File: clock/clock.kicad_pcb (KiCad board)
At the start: 2 copper layers, 100 x 50 mm, 81 parts, among them J1 FTDI, J2 USB, J3 TP, SW1 SW_SPST, SW2 SW_SPST, SW3 SW_SPST, SW4 SW_SPST, SW5 SW_SPST, U1 iv12, U10 PCA9685PW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

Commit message: Clean up
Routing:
- net Net-(R16-Pad2): track 15.8 -> 17.4 mm
- net +5V: track 288.8 -> 287.9 mm
- net Net-(R20-Pad2): track 14.1 -> 14.6 mm

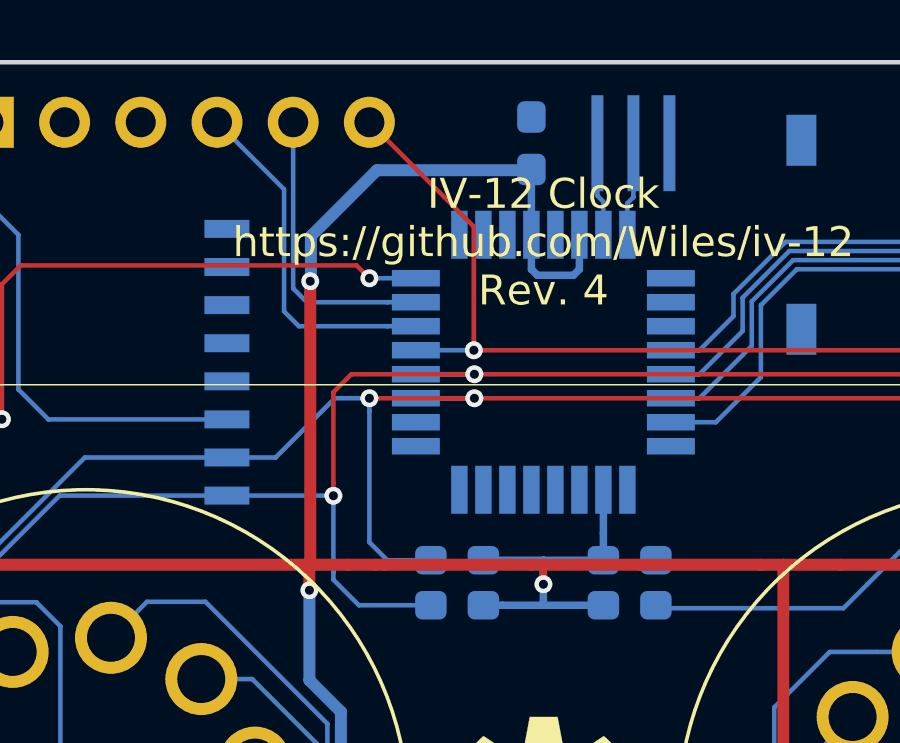
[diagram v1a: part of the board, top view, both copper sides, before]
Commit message: Fixed crystal pinout
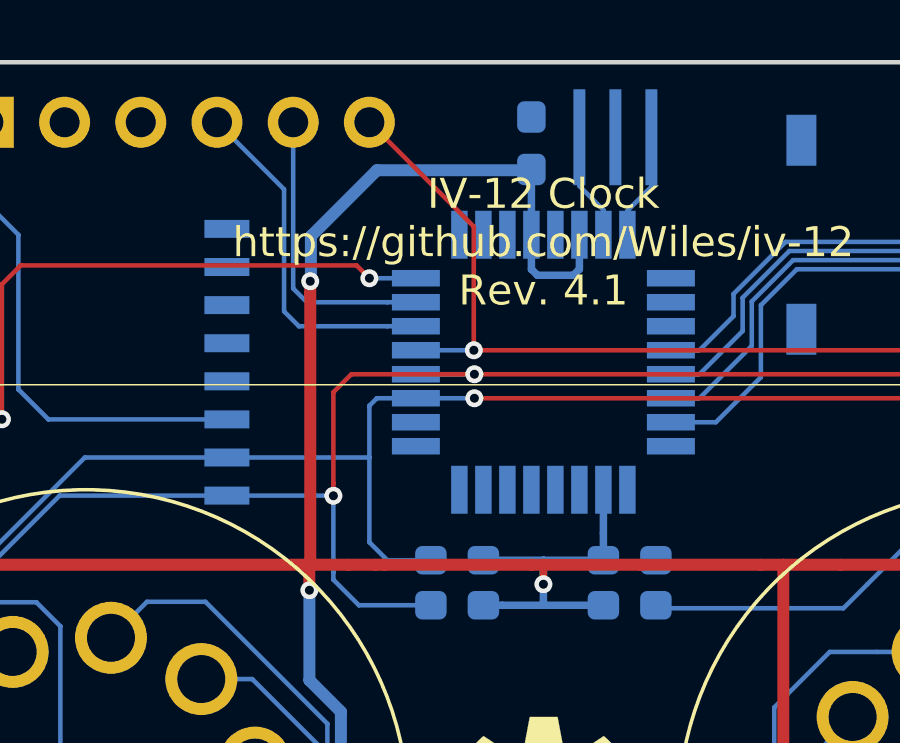
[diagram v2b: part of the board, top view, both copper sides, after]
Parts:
- BT1: value 3v -> CR1220
- R29, R30, R31, R32: value R_Small -> 27
- Y1: value 16MHz -> 16 MHz
- moved Y1 0.63 mm to (129.4, 104.5), turned to 180 degrees
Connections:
- Y1 pad 1: Net-(U11-Pad7) -> Net-(U11-Pad8)
- Y1 pad 2: Net-(U11-Pad8) -> GND
- Y1 pad 3: GND -> Net-(U11-Pad7)
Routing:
- net SDA: track 126.4 -> 123.5 mm, vias 3 -> 2
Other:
- board text added: "IV-12 Clock https://github.com/Wiles/iv-12 Rev. 4.1"
- board text removed: "IV-12 Clock https://github.com/Wiles/iv-12 Rev. 4"

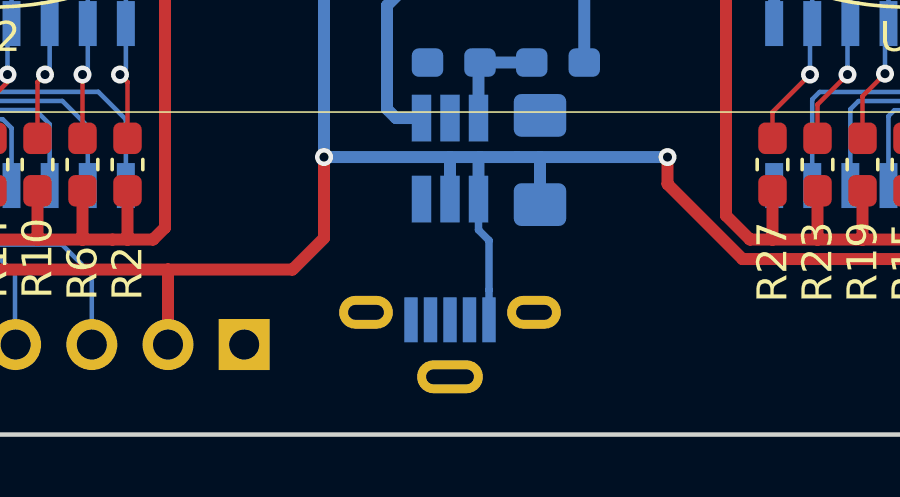
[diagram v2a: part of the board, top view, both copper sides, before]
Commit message: Changed USB footprint
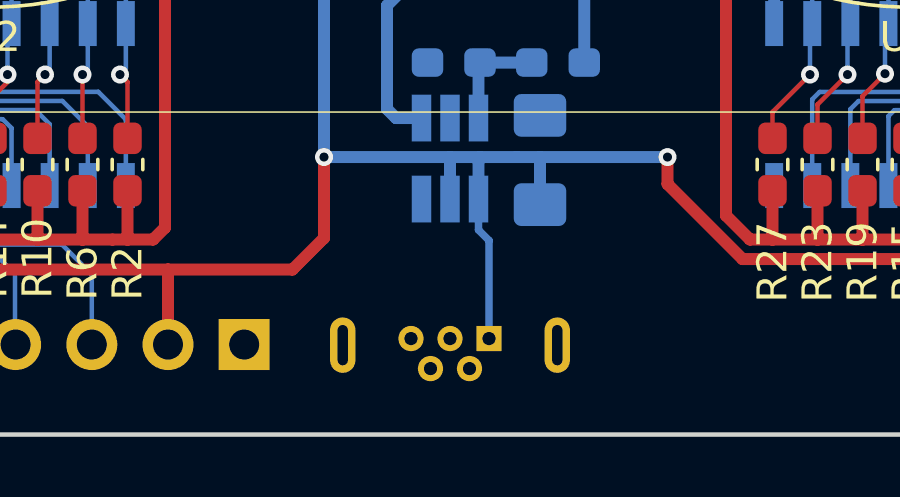
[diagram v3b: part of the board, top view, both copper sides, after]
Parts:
- J2: footprint Connector_USB:USB_Micro-B_Molex-105133-0001 -> Connector_USB:USB_Micro-B_Wuerth_614105150721_Vertical
- moved J2 1.32 mm to (128.3, 148.8)
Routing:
- net +5V: track 287.9 -> 288.5 mm
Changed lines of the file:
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@@
     (thickness 1.6)
     (drawings 16)
-    (tracks 907)
+    (tracks 906)
     (zones 0)
     (modules 81)
@@
     )
   )
-  (module Connector_USB:USB_Micro-B_Molex-105133-0001 (layer B.Cu)
-    (at 127 149 180)
-    (descr "Molex Vertical Micro USB Typ-B (http://www.molex.com/pdm_docs/sd/1051330001_sd.pdf)")
-    (tags "Micro-USB SMD Typ-B Vertical")
-    (attr smd)
-    (fp_text reference J2 (at 0 2.85) (layer B.SilkS) hide
-      (effects (font (size 1 1) (thickness 0.15)) (justify mirror))
-    )
-    (fp_text value USB (at -0.025 -3 180) (layer B.Fab)
-      (effects (font (size 1 1) (thickness 0.15)) (justify mirror))
-    )
-    (fp_text user %R (at 0 0.375 180) (layer B.Fab)
-      (effects (font (size 1 1) (thickness 0.15)) (justify mirror))
-    )
-    (fp_line (start -4 -1.565) (end -4 1.435) (layer B.Fab) (width 0.1))
-    (fp_line (start 4 -1.565) (end 4 1.435) (layer B.Fab) (width 0.1))
-    (fp_line (start -4 -1.565) (end 4 -1.565) (layer B.Fab) (width 0.1))
-    (fp_line (start 4 1.435) (end -4 1.435) (layer B.Fab) (width 0.1))
-    (fp_line (start -1.7 1.075) (end -1.7 1.825) (layer B.SilkS) (width 0.12))
-    (fp_line (start -1.7 1.825) (end -1.1 1.825) (layer B.SilkS) (width 0.12))
-    (fp_line (start -2 1.825) (end -4.15 1.825) (layer B.SilkS) (width 0.12))
-    (fp_line (start 4.15 1.825) (end 4.15 -1.725) (layer B.SilkS) (width 0.12))
-    (fp_line (start -4.15 -1.725) (end -1.25 -1.725) (layer B.SilkS) (width 0.12))
-    (fp_line (start -4.15 1.825) (end -4.15 -1.725) (layer B.SilkS) (width 0.12))
-    (fp_line (start 4.15 -1.725) (end 1.25 -1.725) (layer B.SilkS) (width 0.12))
-    (fp_line (start 2 1.825) (end 4.15 1.825) (layer B.SilkS) (width 0.12))
-    (fp_line (start -1.3 1.675) (end -1.525 1.85) (layer B.Fab) (width 0.1))
-    (fp_line (start -1.525 2.075) (end -1.075 2.075) (layer B.Fab) (width 0.1))
-    (fp_line (start -1.3 1.675) (end -1.075 1.85) (layer B.Fab) (width 0.1))
-    (fp_line (start -1.525 1.85) (end -1.525 2.075) (layer B.Fab) (width 0.1))
-    (fp_line (start -1.075 2.075) (end -1.075 1.85) (layer B.Fab) (width 0.1))
-    (fp_line (start -4.5 -2.13) (end -4.5 2.13) (layer B.CrtYd) (width 0.05))
-    (fp_line (start -4.5 2.13) (end 4.5 2.13) (layer B.CrtYd) (width 0.05))
-    (fp_line (start -4.5 -2.13) (end 4.5 -2.13) (layer B.CrtYd) (width 0.05))
-    (fp_line (start 4.5 -2.13) (end 4.5 2.13) (layer B.CrtYd) (width 0.05))
-    (pad 3 smd rect (at 0 0.825 180) (size 0.45 1.5) (layers B.Cu B.Paste B.Mask)
-      (net 94 "Net-(J2-Pad3)"))
-    (pad 4 smd rect (at 0.65 0.825 180) (size 0.45 1.5) (layers B.Cu B.Paste B.Mask)
-      (net 1 GND))
-    (pad 2 smd rect (at -0.65 0.825 180) (size 0.45 1.5) (layers B.Cu B.Paste B.Mask)
-      (net 105 "Net-(J2-Pad2)"))
-    (pad 5 smd rect (at 1.3 0.825 180) (size 0.45 1.5) (layers B.Cu B.Paste B.Mask)
-      (net 1 GND))
-    (pad 1 smd rect (at -1.3 0.825 180) (size 0.45 1.5) (layers B.Cu B.Paste B.Mask)
-      (net 31 +5V))
-    (pad 6 thru_hole oval (at -2.8 1.075 180) (size 1.8 1.1) (drill oval 1.2 0.5) (layers *.Cu *.Mask)
-      (net 1 GND))
-    (pad 6 thru_hole oval (at 2.8 1.075 180) (size 1.8 1.1) (drill oval 1.2 0.5) (layers *.Cu *.Mask)
-      (net 1 GND))
-    (pad 6 thru_hole oval (at 0 -1.075 180) (size 2.2 1.1) (drill oval 1.6 0.5) (layers *.Cu *.Mask)
-      (net 1 GND))
-    (model ${KISYS3DMOD}/Connector_USB.3dshapes/USB_Micro-B_Molex-105133-0001.wrl
-      (at (xyz 0 0 0))
-      (scale (xyz 1 1 1))
-      (rotate (xyz 0 0 0))
-    )
-  )
   (module Connector_PinHeader_2.54mm:PinHeader_1x05_P2.54mm_Vertical (layer B.Cu)
     (at 120.14 149 90)
@@
     )
   )
+  (module Connector_USB:USB_Micro-B_Wuerth_614105150721_Vertical (layer B.Cu)
+    (at 128.3 148.8 180)
+    (descr "USB Micro-B receptacle, through-hole, vertical, http://katalog.we-online.de/em/datasheet/614105150721.pdf")
+    (tags "usb micro receptacle vertical")
+    (fp_text reference J2 (at 1.3 2.48 180) (layer B.SilkS)
+      (effects (font (size 1 1) (thickness 0.15)) (justify mirror))
+    )
+    (fp_text value USB (at 1.3 -2.92 180) (layer B.Fab)
+      (effects (font (size 1 1) (thickness 0.15)) (justify mirror))
+    )
+    (fp_line (start -2.7 1.23) (end -1 1.23) (layer B.Fab) (width 0.15))
+    (fp_line (start -1 1.23) (end 0 0.23) (layer B.Fab) (width 0.15))
+    (fp_line (start 0 0.23) (end 1 1.23) (layer B.Fab) (width 0.15))
+    (fp_line (start 1 1.23) (end 5.3 1.23) (layer B.Fab) (width 0.15))
+    (fp_line (start 5.3 1.23) (end 5.3 -1.67) (layer B.Fab) (width 0.15))
+    (fp_line (start 5.3 -1.67) (end -2.7 -1.67) (layer B.Fab) (width 0.15))
+    (fp_line (start -2.7 -1.67) (end -2.7 1.23) (layer B.Fab) (width 0.15))
+    (fp_line (start -2.85 0.905) (end -2.85 1.38) (layer B.SilkS) (width 0.15))
+    (fp_line (start -2.85 1.38) (end 5.45 1.38) (layer B.SilkS) (width 0.15))
+    (fp_line (start 5.45 1.38) (end 5.45 0.905) (layer B.SilkS) (width 0.15))
+    (fp_line (start -2.85 -1.345) (end -2.85 -1.82) (layer B.SilkS) (width 0.15))
+    (fp_line (start -2.85 -1.82) (end 5.45 -1.82) (layer B.SilkS) (width 0.15))
+    (fp_line (start 5.45 -1.82) (end 5.45 -1.345) (layer B.SilkS) (width 0.15))
+    (fp_line (start -1 1.68) (end 1 1.68) (layer B.SilkS) (width 0.15))
+    (fp_line (start -3.2 1.73) (end -3.2 -2.17) (layer B.CrtYd) (width 0.05))
+    (fp_line (start -3.2 -2.17) (end 5.8 -2.17) (layer B.CrtYd) (width 0.05))
+    (fp_line (start 5.8 -2.17) (end 5.8 1.73) (layer B.CrtYd) (width 0.05))
+    (fp_line (start 5.8 1.73) (end -3.2 1.73) (layer B.CrtYd) (width 0.05))
+    (fp_text user %R (at 1.3 -0.22 180) (layer B.Fab)
+      (effects (font (size 1 1) (thickness 0.15)) (justify mirror))
+    )
+    (pad 1 thru_hole rect (at 0 0 180) (size 0.84 0.84) (drill 0.44) (layers *.Cu *.Mask)
+      (net 31 +5V))
+    (pad 2 thru_hole circle (at 0.65 -1 180) (size 0.84 0.84) (drill 0.44) (layers *.Cu *.Mask)
+      (net 105 "Net-(J2-Pad2)"))
+    (pad 3 thru_hole circle (at 1.3 0 180) (size 0.84 0.84) (drill 0.44) (layers *.Cu *.Mask)
+      (net 94 "Net-(J2-Pad3)"))
+    (pad 4 thru_hole circle (at 1.95 -1 180) (size 0.84 0.84) (drill 0.44) (layers *.Cu *.Mask)
+      (net 1 GND))
+    (pad 5 thru_hole circle (at 2.6 0 180) (size 0.84 0.84) (drill 0.44) (layers *.Cu *.Mask)
+      (net 1 GND))
+    (pad 6 thru_hole oval (at -2.275 -0.22 180) (size 0.85 1.85) (drill oval 0.35 1.35) (layers *.Cu *.Mask)
+      (net 1 GND))
+    (pad 6 thru_hole oval (at 4.875 -0.22 180) (size 0.85 1.85) (drill oval 0.35 1.35) (layers *.Cu *.Mask)
+      (net 1 GND))
+    (model ${KISYS3DMOD}/Connector_USB.3dshapes/USB_Micro-B_Wuerth_614105150721_Vertical.wrl
+      (at (xyz 0 0 0))
+      (scale (xyz 1 1 1))
+      (rotate (xyz 0 0 0))
+    )
+  )
   (gr_text + (at 133.5 124.2) (layer B.SilkS)
     (effects (font (size 1 1) (thickness 0.15)) (justify mirror))
@@
   (segment (start 121.4 118.75) (end 121.7 118.75) (width 0.4) (layer F.Cu) (net 31))
   (segment (start 120.5 118.75) (end 121.4 118.75) (width 0.4) (layer F.Cu) (net 31))
-  (segment (start 128.3 147.175) (end 128.3 148.175) (width 0.25) (layer B.Cu) (net 31))
-  (segment (start 128.3 145.53) (end 128.3 147.175) (width 0.25) (layer B.Cu) (net 31))
   (segment (start 127.95 145.18) (end 128.3 145.53) (width 0.25) (layer B.Cu) (net 31))
   (segment (start 127.95 144.15) (end 127.95 145.18) (width 0.25) (layer B.Cu) (net 31))
@@
   (segment (start 81 127) (end 80 126) (width 0.4) (layer F.Cu) (net 31))
   (via (at 122.8 142.749984) (size 0.6) (drill 0.3) (layers F.Cu B.Cu) (net 31))
-  (segment (start 123.224264 142.749984) (end 122.8 142.749984) (width 0.4) (layer B.Cu) (net 31))
-  (segment (start 126.999984 142.749984) (end 123.224264 142.749984) (width 0.4) (layer B.Cu) (net 31))
   (segment (start 127 142.75) (end 126.999984 142.749984) (width 0.4) (layer B.Cu) (net 31))
   (segment (start 121.7 118.75) (end 126.6 118.75) (width 0.4) (layer F.Cu) (net 31))
@@
   (segment (start 134.25 142.75) (end 134.25 143.65) (width 0.4) (layer F.Cu) (net 31))
   (segment (start 134.25 143.65) (end 136.75 146.15) (width 0.4) (layer F.Cu) (net 31))
+  (segment (start 126.999984 142.749984) (end 123.224264 142.749984) (width 0.4) (layer B.Cu) (net 31))
+  (segment (start 123.224264 142.749984) (end 122.8 142.749984) (width 0.4) (layer B.Cu) (net 31))
+  (segment (start 128.3 148.8) (end 128.3 145.53) (width 0.25) (layer B.Cu) (net 31))
   (segment (start 143.125 132.776301) (end 143.0861 132.815201) (width 0.152) (layer B.Cu) (net 32) (status 30))
   (segment (start 143.125 128.5) (end 143.125 132.776301) (width 0.152) (layer B.Cu) (net 32) (status 30))

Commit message: Label Tx and Rx pins
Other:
- board text added: "R"
- board text added: "T"
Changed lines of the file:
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@@
   (general
     (thickness 1.6)
-    (drawings 16)
+    (drawings 18)
     (tracks 906)
     (zones 0)
@@
     )
   )
+  (gr_text R (at 116.1 106 90) (layer B.SilkS)
+    (effects (font (size 1 1) (thickness 0.15)) (justify mirror))
+  )
+  (gr_text T (at 118.7 106 90) (layer B.SilkS)
+    (effects (font (size 1 1) (thickness 0.15)) (justify mirror))
+  )
   (gr_text + (at 133.5 124.2) (layer B.SilkS)

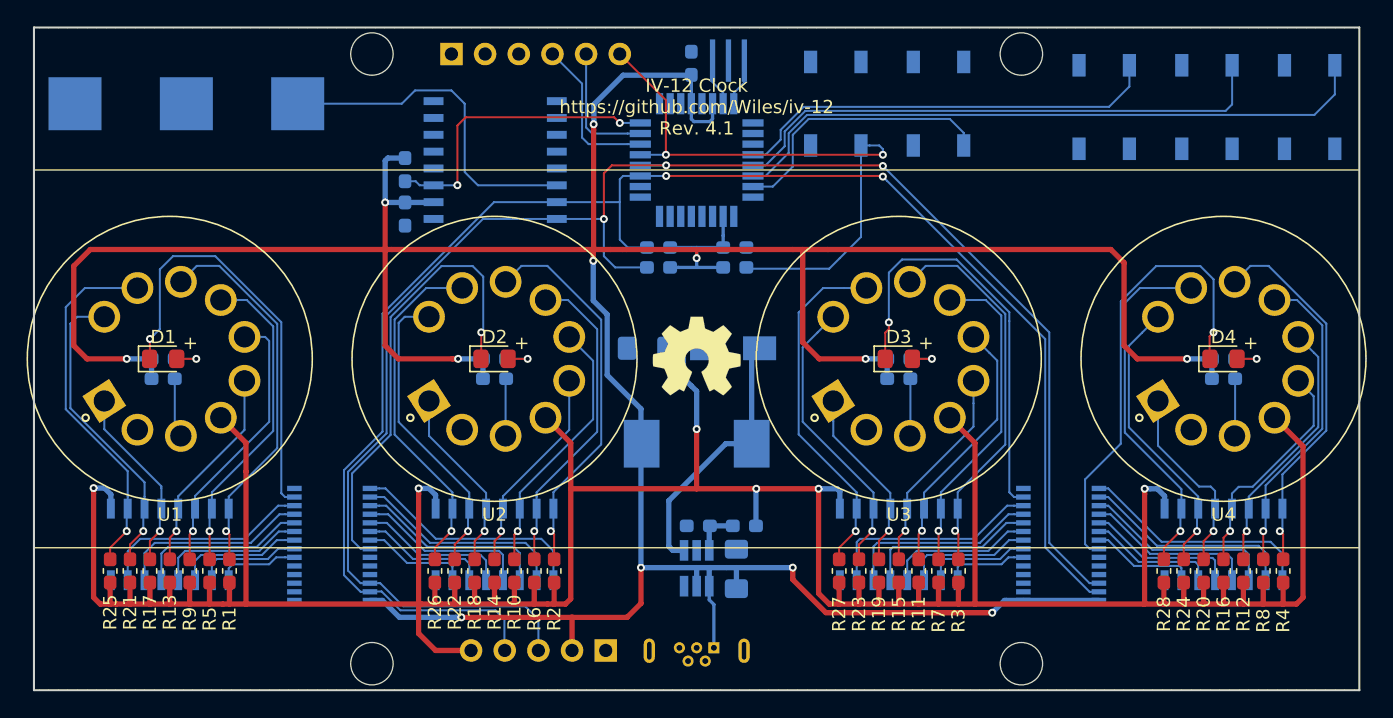
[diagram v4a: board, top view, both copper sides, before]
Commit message: Added capacitor to reset line
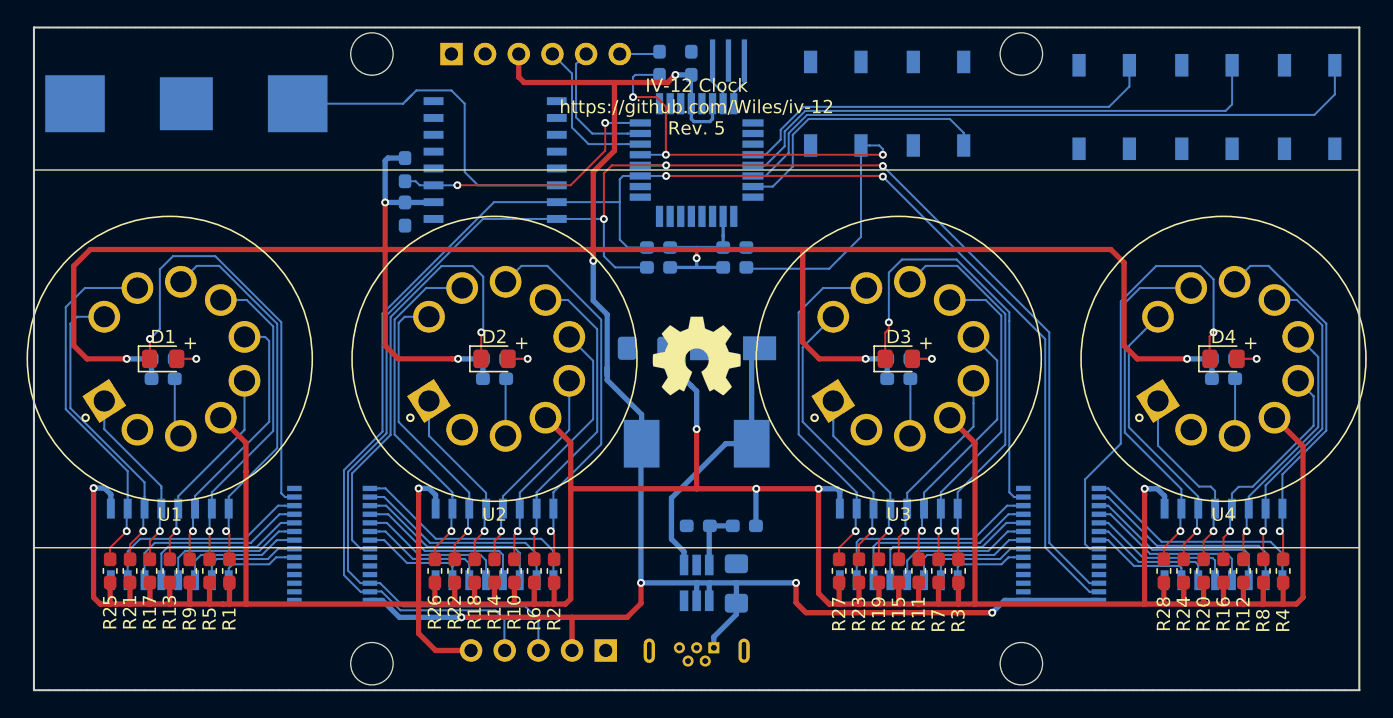
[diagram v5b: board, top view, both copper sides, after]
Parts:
- added C5: 1u, Capacitor_SMD:C_0603_1608Metric_Pad1.05x0.95mm_HandSolder, B.Cu at (124.2, 104.7)
- moved C1 1.10 mm to (130.0, 143.9)
- moved U13 1.10 mm to (127.0, 143.9)
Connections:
- J1 pad 3: Net-(J1-Pad3) -> +5V
- J1 pad 6: RST -> Net-(C5-Pad2)
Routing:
- net +5V: track 288.5 -> 298.7 mm
- net Net-(C5-Pad2): track 0.00 -> 3.07 mm
- net SQW: track 22.8 -> 21.1 mm
- net RST: track 46.1 -> 47.4 mm, vias 2 -> 3
- net Net-(R37-Pad2): track 3.60 -> 4.77 mm
- net TX: track 9.82 -> 10.5 mm
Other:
- net class Power: trace_width 0.25 -> 0.4
- board text added: "IV-12 Clock https://github.com/Wiles/iv-12 Rev. 5"
- board text removed: "IV-12 Clock https://github.com/Wiles/iv-12 Rev. 4.1"
